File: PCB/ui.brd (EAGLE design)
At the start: 68 x 42.2 mm, 29 parts

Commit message: UI PCB finished and slickscreen checked
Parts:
- added R8, R9: (no value), rcl:R0603
- moved C4 0.57 mm to (21.1, 7.87)
- moved C5 0.51 mm to (21.1, 3.81)
- renumbered RN1 to R10, RN2 to R12, RN3 to R14, RN4 to R11, RN5 to R13, RN6 to R15, U$1 to IC3, U$2 to IC4, U$3 to D2, U$4 to IC1, U$5 to IC2, U$6 to D1
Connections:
- new net SYNC: IC3.6, IC4.6, J1.6, R8.1, R9.2
- net +3V3: now also R8.2
- net GND: now also R9.1
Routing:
- net SYNC: track 0.00 -> 69.6 mm, vias 0 -> 5
- net +3V3: track 251.4 -> 260.5 mm
- net GND: track 24.4 -> 25.5 mm
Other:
- board text removed: "DMX to DMX controller"

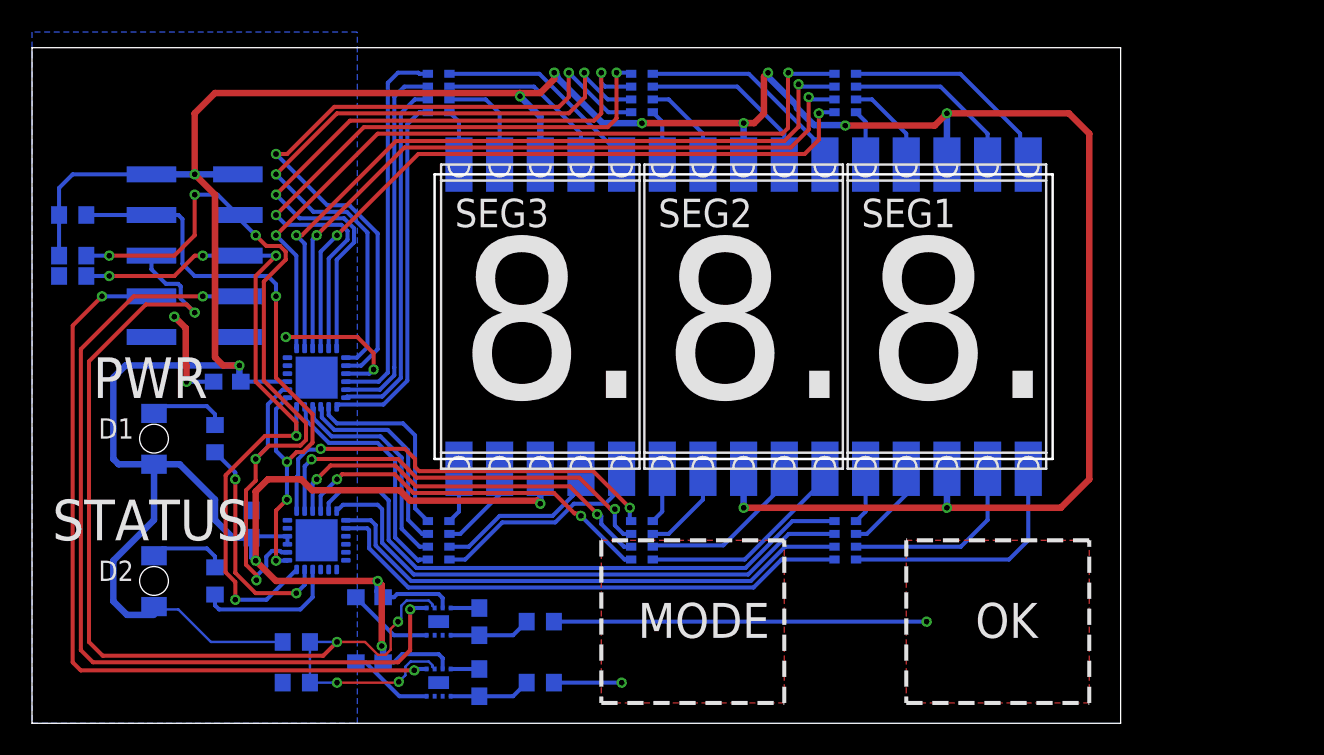
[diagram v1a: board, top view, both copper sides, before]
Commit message: Minor changes to fron PCB. changed positioning of segments and buttons
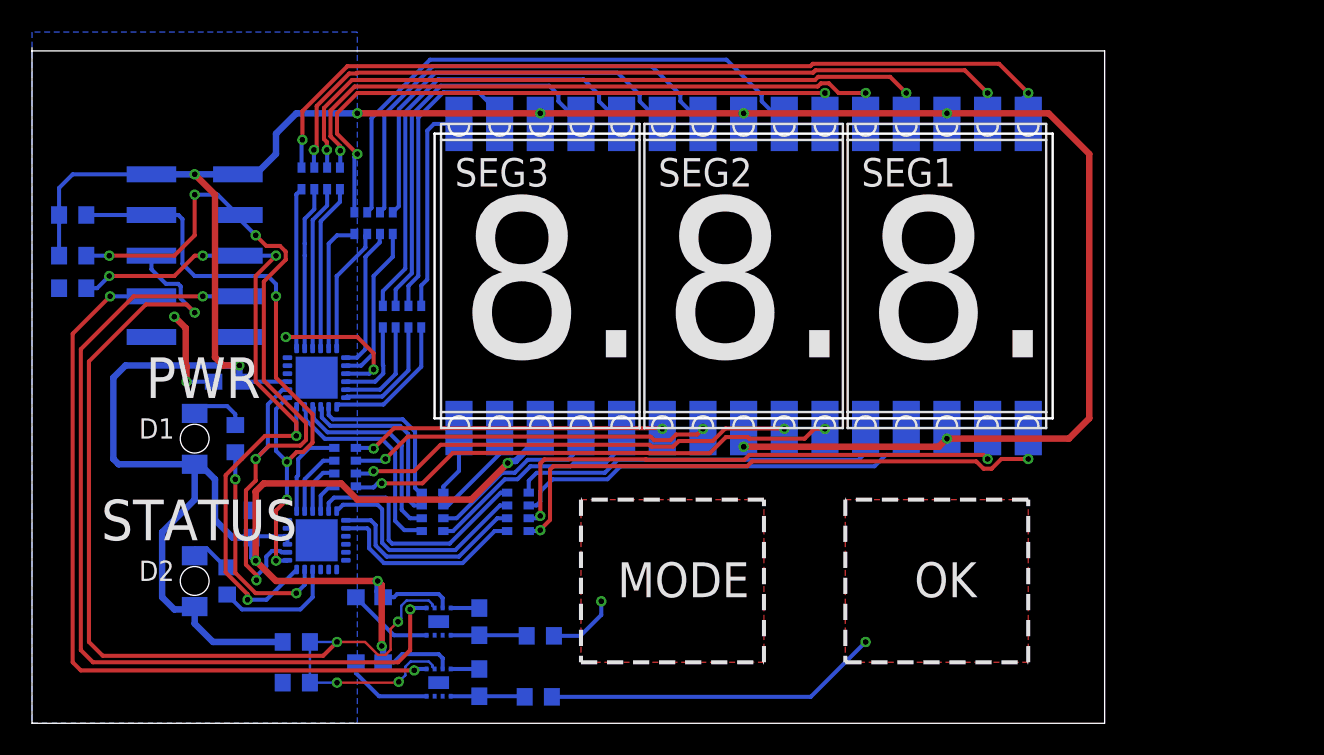
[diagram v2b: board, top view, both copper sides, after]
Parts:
- moved R10 33.2 mm to (18.0, 34.0), turned to 0 degrees
- moved R11 20.5 mm to (30.4, 13.2)
- moved R13 19.1 mm to (19.6, 16.0)
- moved R12 18.6 mm to (21.3, 31.2), turned to 0 degrees
- moved R14 14.2 mm to (23.1, 25.4), turned to 0 degrees
- moved SEG1 2.54 mm to (57.1, 27.9)
- moved SEG2 2.54 mm to (44.5, 27.9)
- moved SEG3 2.54 mm to (31.8, 27.9)
- moved D1 2.54 mm to (10.2, 17.8)
- moved D2 2.54 mm to (10.2, 8.89)
- moved R15 1.82 mm to (25.0, 13.2)
- moved R3 1.27 mm to (12.7, 17.8)
- moved R1 0.90 mm to (31.6, 1.65)
- moved R2 0.89 mm to (31.8, 5.46)
- moved R4 0.76 mm to (12.2, 8.89)
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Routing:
- net N$4: track 13.9 -> 53.2 mm, vias 0 -> 2
- net SEGMENTA1: track 48.7 -> 10.1 mm, vias 2 -> 0
- net N$3: track 11.4 -> 49.3 mm, vias 0 -> 2
- net N$2: track 5.95 -> 43.3 mm, vias 0 -> 2
- net N$1: track 3.52 -> 40.1 mm, vias 0 -> 2
- net SEGMENTA0: track 46.4 -> 10.2 mm, vias 2 -> 0
- net SEGMENTB6: track 44.2 -> 10.0 mm, vias 2 -> 0
- net SEGMENTA5: track 44.3 -> 10.3 mm, vias 2 -> 0
- net SEGMENTB5: track 42.6 -> 9.02 mm, vias 2 -> 0
- net SEGMENTB0: track 41.3 -> 7.95 mm, vias 2 -> 0
- net SEGMENTA6: track 42.7 -> 10.4 mm, vias 2 -> 0
- net SEGMENTB1: track 40.3 -> 8.40 mm, vias 2 -> 0
- net +3V3: track 260.5 -> 230.2 mm, vias 15 -> 12
- net N$8: track 13.6 -> 39.7 mm, vias 0 -> 2
- net N$7: track 11.4 -> 35.2 mm
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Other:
- board size 68 x 42.2 mm -> 67 x 42.2 mm
